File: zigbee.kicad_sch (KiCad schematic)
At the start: 49 parts, among them J201 Conn_Coaxial, J202 Conn_Coaxial, U201 0900PC15A0036E, U202 CC2652P1FRGZR, U203 CC2652P1FRGZR, X201 Crystal, X202 Crystal_GND24

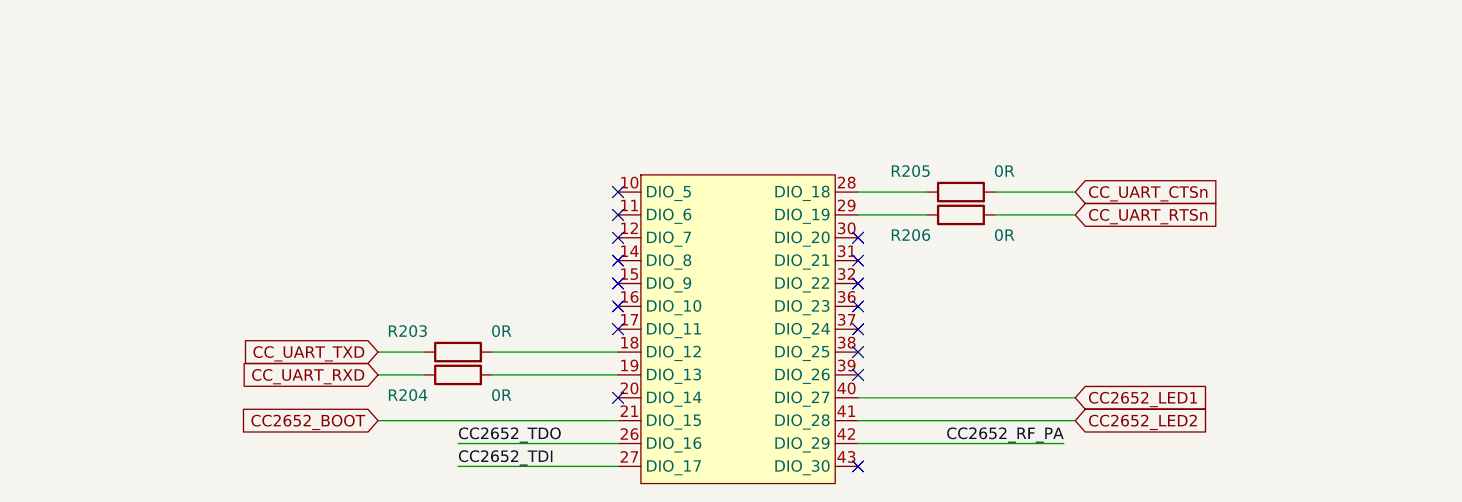
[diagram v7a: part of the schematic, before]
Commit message: Added eMMc
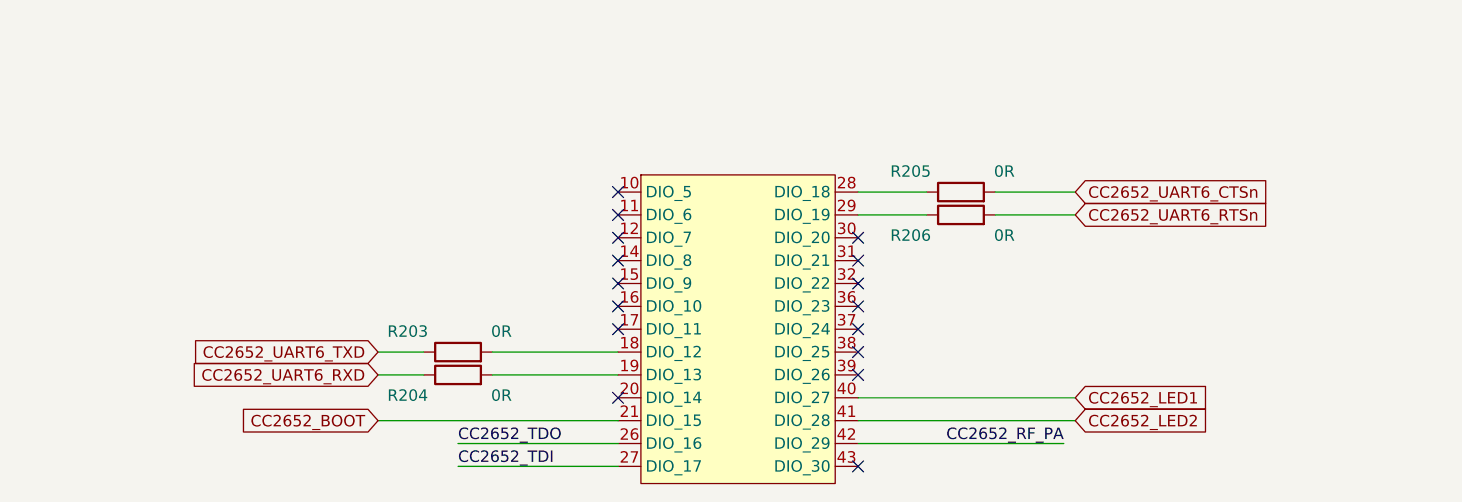
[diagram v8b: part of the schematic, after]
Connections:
- net CC_UART_CTSn renamed CC2652_UART6_CTSn
- net CC_UART_RTSn renamed CC2652_UART6_RTSn
- net CC_UART_RXD renamed CC2652_UART6_RXD
- net CC_UART_TXD renamed CC2652_UART6_TXD
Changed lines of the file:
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@@
 		)
 	)
-	(global_label "CC_UART_RXD"
+	(global_label "CC2652_UART6_RXD"
 		(shape input)
 		(at 76.2 251.46 180)
@@
 		)
 		(property "Intersheetrefs" "${INTERSHEET_REFS}"
-			(at 60.3334 251.46 0)
+			(at 54.2859 251.46 0)
 			(effects
 				(font
@@
 		)
 	)
-	(global_label "CC_UART_TXD"
+	(global_label "CC2652_UART6_TXD"
 		(shape input)
 		(at 76.2 248.92 180)
@@
 		)
 		(property "Intersheetrefs" "${INTERSHEET_REFS}"
-			(at 60.6358 248.92 0)
+			(at 54.5883 248.92 0)
 			(effects
 				(font
@@
 		)
 	)
-	(global_label "CC_UART_RTSn"
+	(global_label "CC2652_UART6_RTSn"
 		(shape input)
 		(at 153.67 233.68 0)
@@
 		)
 		(property "Intersheetrefs" "${INTERSHEET_REFS}"
-			(at 170.3832 233.68 0)
+			(at 176.4307 233.68 0)
 			(effects
 				(font
@@
 		)
 	)
-	(global_label "CC_UART_CTSn"
+	(global_label "CC2652_UART6_CTSn"
 		(shape input)
 		(at 153.67 231.14 0)
@@
 		)
 		(property "Intersheetrefs" "${INTERSHEET_REFS}"
-			(at 170.3832 231.14 0)
+			(at 176.4307 231.14 0)
 			(effects
 				(font
